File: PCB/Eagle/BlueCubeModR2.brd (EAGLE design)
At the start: 38.6 x 22.1 mm, 33 parts, among them J3 2174507-2, U1 ESP32-PICO-D4, U2 CP2104-F03-GM, U4 STBC08, U7 NCP161

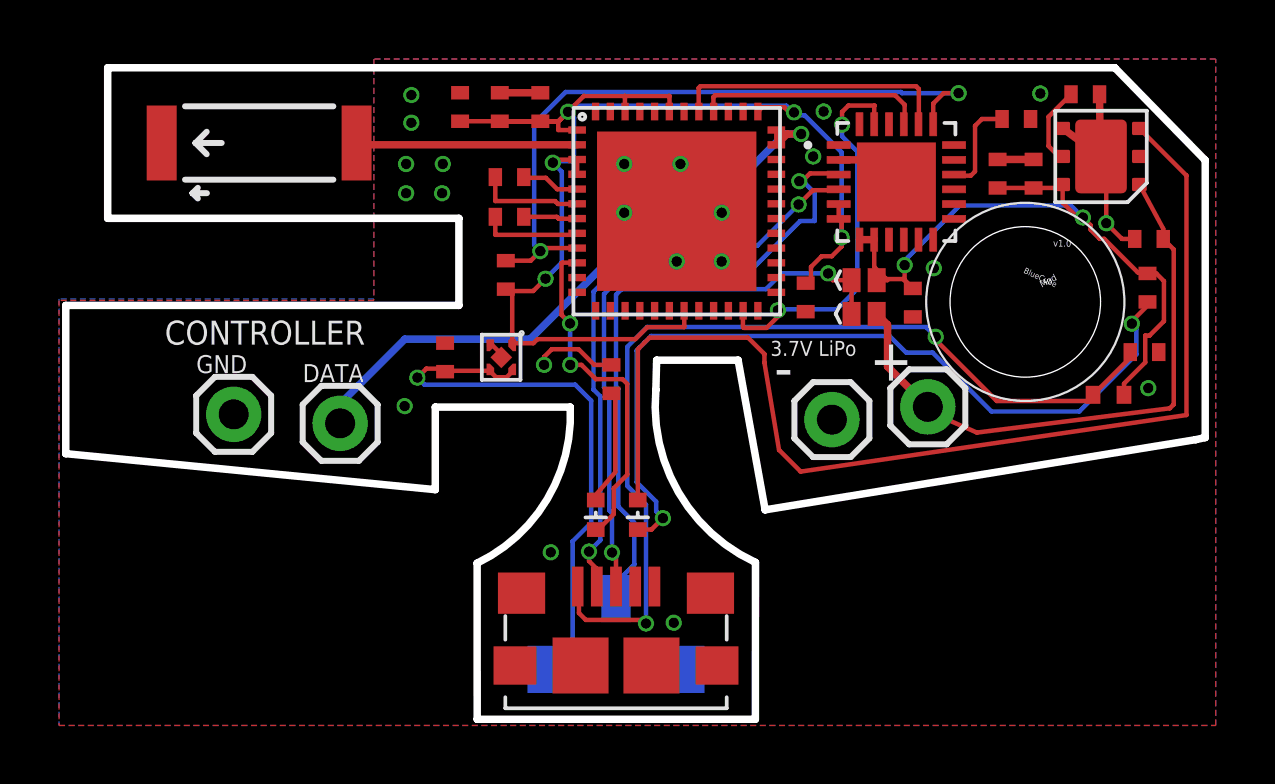
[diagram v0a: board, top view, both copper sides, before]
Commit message: Added v2 firmware w/ switch support
see updated readme for new build instructions
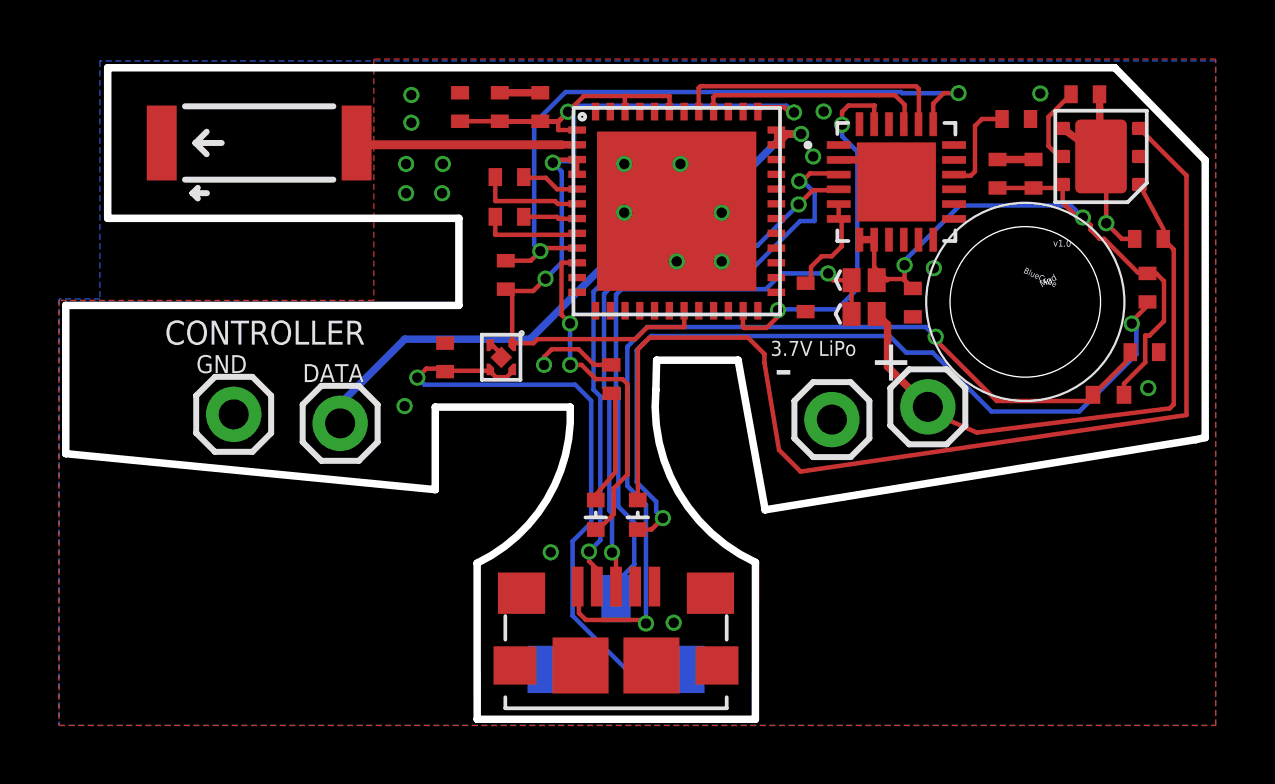
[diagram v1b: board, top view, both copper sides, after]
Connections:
- new net 3.3V_USB: C10.1, U2.5, U2.6
- net 3.3V: no longer C10.1, U2.5, U2.6
- net PWRIN: now also S2.1; no longer S2.3
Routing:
- net 3.3V: track 48.1 -> 39.7 mm, vias 5 -> 4
- net 3.3V_USB: track 0.00 -> 3.43 mm
- net PWRIN: track 19.6 -> 22.1 mm
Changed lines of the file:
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@@
 </polygon>
 <polygon width="0.1524" layer="16">
-<vertex x="-30.4546" y="29.21"/>
-<vertex x="-30.4546" y="21.082"/>
+<vertex x="-39.7383" y="29.1465"/>
+<vertex x="-39.7383" y="21.082"/>
 <vertex x="-41.1226" y="21.082"/>
 <vertex x="-41.1226" y="6.6294"/>
 <vertex x="-1.9304" y="6.6294"/>
-<vertex x="-1.9304" y="29.21"/>
+<vertex x="-1.9304" y="29.1465"/>
 </polygon>
 <contactref element="C11" pad="1"/>
@@
 <via x="-29.1846" y="27.051" extent="1-16" drill="0.35"/>
 <polygon width="0.1524" layer="2">
-<vertex x="-30.4546" y="29.1338"/>
-<vertex x="-30.4546" y="21.1074"/>
+<vertex x="-39.7383" y="29.1338"/>
+<vertex x="-39.7383" y="21.1074"/>
 <vertex x="-41.0718" y="21.1074"/>
 <vertex x="-41.0718" y="6.477"/>
@@
 </polygon>
 <polygon width="0.1524" layer="15">
-<vertex x="-30.4546" y="29.1592"/>
-<vertex x="-30.4546" y="21.082"/>
+<vertex x="-39.7256" y="29.1592"/>
+<vertex x="-39.7256" y="21.082"/>
 <vertex x="-41.1226" y="21.082"/>
 <vertex x="-41.1226" y="6.477"/>
@@
 <wire x1="-25.7668" y1="18.6168125" x2="-25.7668" y2="18.6208" width="0.1524" layer="1"/>
 <wire x1="-25.7668" y1="18.6168125" x2="-25.95530625" y2="18.42830625" width="0.1524" layer="1"/>
-<wire x1="-23.7208" y1="9.5578" x2="-23.7208" y2="12.87083125" width="0.1524" layer="16"/>
+<wire x1="-23.7208" y1="12.87083125" x2="-23.7208" y2="10.3452" width="0.1524" layer="16"/>
 <wire x1="-26.5068" y1="18.6208" x2="-26.31430625" y2="18.42830625" width="0.1524" layer="1"/>
 <wire x1="-26.31430625" y1="18.42830625" x2="-25.95530625" y2="18.42830625" width="0.1524" layer="1"/>
@@
 <wire x1="-28.9814" y1="18.415" x2="-28.677" y2="18.7194" width="0.1524" layer="1"/>
 <wire x1="-28.1428" y1="18.7194" x2="-28.0412" y2="18.6178" width="0.1524" layer="1"/>
-<contactref element="S2" pad="3"/>
-<wire x1="-24.7504" y1="8.5282" x2="-23.7208" y2="9.5578" width="0.1524" layer="16"/>
+<contactref element="S2" pad="1"/>
+<wire x1="-23.7208" y1="10.3452" x2="-21.9038" y2="8.5282" width="0.1524" layer="16"/>
+<wire x1="-21.9038" y1="8.5282" x2="-19.7504" y2="8.5282" width="0.1524" layer="16"/>
 </signal>
 <signal name="3.3V">
@@
 <wire x1="-19.9372" y1="20.1252" x2="-21.18934375" y2="20.1252" width="0.1524" layer="1"/>
 <wire x1="-21.59574375" y1="19.7188" x2="-24.9098" y2="19.7188" width="0.1524" layer="1"/>
-<contactref element="U2" pad="6"/>
-<contactref element="U2" pad="5"/>
 <wire x1="-24.8158" y1="27.101" x2="-24.1987" y2="27.101" width="0.1524" layer="1"/>
 <wire x1="-24.1987" y1="27.101" x2="-23.876" y2="27.4237" width="0.1524" layer="1"/>
@@
 <wire x1="-26.1874" y1="27.101" x2="-26.188" y2="27.1016" width="0.1524" layer="1"/>
 <wire x1="-21.18934375" y1="20.1252" x2="-21.59574375" y2="19.7188" width="0.1524" layer="1"/>
-<contactref element="C10" pad="1"/>
-<wire x1="-14.7058" y1="23.7944" x2="-14.7058" y2="24.2944" width="0.1524" layer="1"/>
-<via x="-14.605" y="23.1648" extent="1-16" drill="0.35"/>
-<wire x1="-15.8584125" y1="27.3022" x2="-16.1205875" y2="27.3022" width="0.1524" layer="16"/>
-<wire x1="-16.1205875" y1="27.3022" x2="-16.2193875" y2="27.401" width="0.1524" layer="16"/>
-<wire x1="-14.605" y1="23.1648" x2="-14.605" y2="26.0487875" width="0.1524" layer="16"/>
-<wire x1="-14.605" y1="26.0487875" x2="-15.8584125" y2="27.3022" width="0.1524" layer="16"/>
 <wire x1="-23.876" y1="27.4237" x2="-23.3419" y2="27.9578" width="0.1524" layer="1"/>
 <wire x1="-23.3419" y1="27.9578" x2="-21.9492" y2="27.9578" width="0.1524" layer="1"/>
@@
 <wire x1="-24.9098" y1="19.7188" x2="-25.0478" y2="19.5808" width="0.1524" layer="1"/>
 <wire x1="-25.0478" y1="19.5808" x2="-25.7668" y2="19.5808" width="0.1524" layer="1"/>
-<wire x1="-14.605" y1="22.86" x2="-14.605" y2="23.1648" width="0.1524" layer="1"/>
-<wire x1="-15.8242" y1="21.6154" x2="-15.6436" y2="21.796" width="0.1524" layer="1"/>
-<wire x1="-15.6436" y1="21.796" x2="-15.6436" y2="22.1653875" width="0.1524" layer="1"/>
-<wire x1="-15.6436" y1="22.1653875" x2="-15.2819875" y2="22.527" width="0.1524" layer="1"/>
-<wire x1="-15.2819875" y1="22.527" x2="-14.938" y2="22.527" width="0.1524" layer="1"/>
-<wire x1="-14.938" y1="22.527" x2="-14.605" y2="22.86" width="0.1524" layer="1"/>
-<wire x1="-14.605" y1="23.1648" x2="-14.605" y2="23.6936" width="0.1524" layer="1"/>
-<wire x1="-14.605" y1="23.6936" x2="-14.7058" y2="23.7944" width="0.1524" layer="1"/>
 <contactref element="R1" pad="1"/>
 <wire x1="-25.9842" y1="21.4122" x2="-25.9842" y2="21.3491" width="0.1524" layer="1"/>
@@
 <contactref element="U1" pad="P$2"/>
 <contactref element="U$1" pad="FEED"/>
-<wire x1="-23.5682" y1="26.3042" x2="-30.9778" y2="26.3042" width="0.254" layer="1"/>
-<wire x1="-31.0388" y1="26.3652" x2="-30.9778" y2="26.3042" width="0.254" layer="1"/>
+<wire x1="-30.9778" y1="26.3042" x2="-31.0388" y2="26.3652" width="0.3048" layer="1"/>
+<wire x1="-23.5682" y1="26.3042" x2="-24.0767" y2="26.3042" width="0.254" layer="1"/>
+<wire x1="-24.0767" y1="26.3042" x2="-24.0792" y2="26.3017" width="0.254" layer="1"/>
+<wire x1="-24.0767" y1="26.3042" x2="-30.9778" y2="26.3042" width="0.3048" layer="1"/>
 </signal>
 <signal name="D+">
@@
 <wire x1="-9.852" y1="27.178" x2="-10.086" y2="26.944" width="0.1524" layer="1"/>
 </signal>
+<signal name="3.3V_USB">
+<contactref element="U2" pad="6"/>
+<contactref element="U2" pad="5"/>
+<contactref element="C10" pad="1"/>
+<wire x1="-14.7058" y1="23.7944" x2="-14.7058" y2="24.2944" width="0.1524" layer="1"/>
+<wire x1="-15.8242" y1="21.6154" x2="-15.6436" y2="21.796" width="0.1524" layer="1"/>
+<wire x1="-15.6436" y1="21.796" x2="-15.6436" y2="22.1653875" width="0.1524" layer="1"/>
+<wire x1="-15.6436" y1="22.1653875" x2="-15.2819875" y2="22.527" width="0.1524" layer="1"/>
+<wire x1="-15.2819875" y1="22.527" x2="-14.938" y2="22.527" width="0.1524" layer="1"/>
+<wire x1="-14.938" y1="22.527" x2="-14.605" y2="22.86" width="0.1524" layer="1"/>
+<wire x1="-14.605" y1="22.86" x2="-14.605" y2="23.6936" width="0.1524" layer="1"/>
+<wire x1="-14.605" y1="23.6936" x2="-14.7058" y2="23.7944" width="0.1524" layer="1"/>
+</signal>
 </signals>
